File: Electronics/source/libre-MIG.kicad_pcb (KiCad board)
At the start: 2 copper layers, 159.5 x 100.9 mm, 136 parts, among them J1 Conn_01x05, J10 Conn_01x03, J11 Conn_01x08, J12 Conn_01x08, J13 Conn_01x05, J14 Conn_01x03, J15 Conn_01x06, J16 Conn_01x02, J17 Conn_01x06, J18 Conn_01x03, J19 Conn_01x08, J2 Conn_01x03, J20 Conn_01x03, J21 Conn_01x08, J3 Conn_01x03, J4 Conn_01x05, J5 Conn_01x05, J6 Conn_01x20, J7 Conn_01x20, J8 Conn_01x03, J9 Conn_01x03, P1 USB_C_Plug_USB2.0, SW1 SW_Push, SW10 SW_Push, SW11 SW_Push, SW12 SW_Push, SW13 SW_Push, SW14 SW_Coded, SW15 RKJXV1220, SW16 SW_Push, SW17 SKRHABE010, SW18 SKRHABE010, SW2 SW_Push, SW3 SW_Push, SW4 SW_Push, SW5 SW_SPDT, SW6 SW_SPDT, SW7 SW_SPDT, SW8 SW_Push, SW9 SW_Push, U1 STM32F030C8Tx, U2 TCA9535PWR, U3 TCA9535PWR, U4 FT231XS, U5 ADP122AUJZ-3.3-R7, U6 MAX11615EEE, Y1 ABL-32.000MHZ-B2

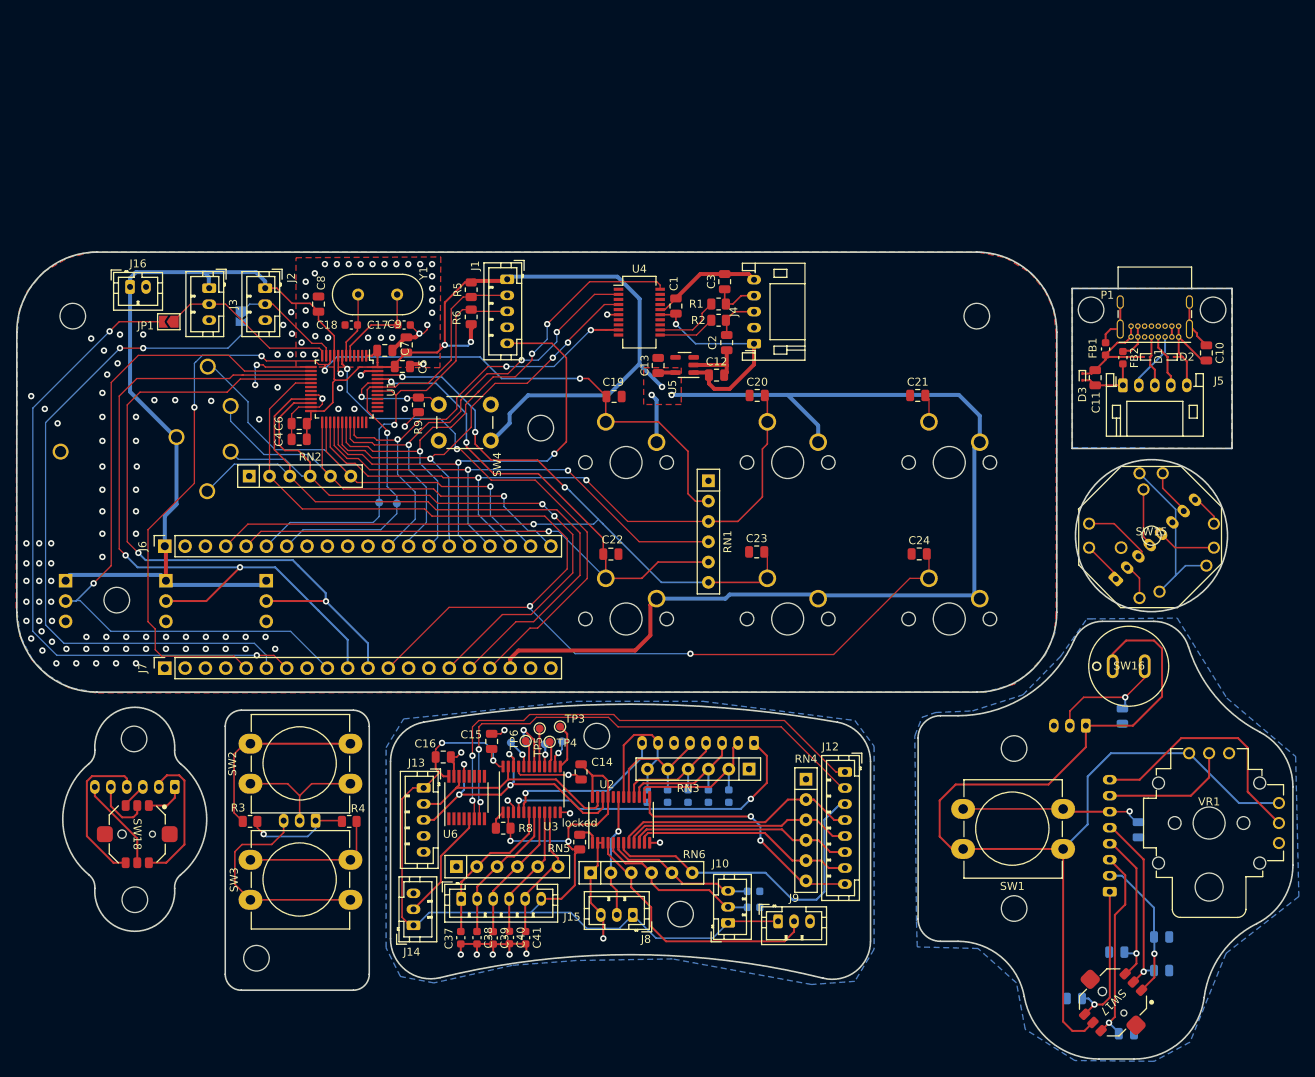
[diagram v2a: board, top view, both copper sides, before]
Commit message: added mechanical ignore
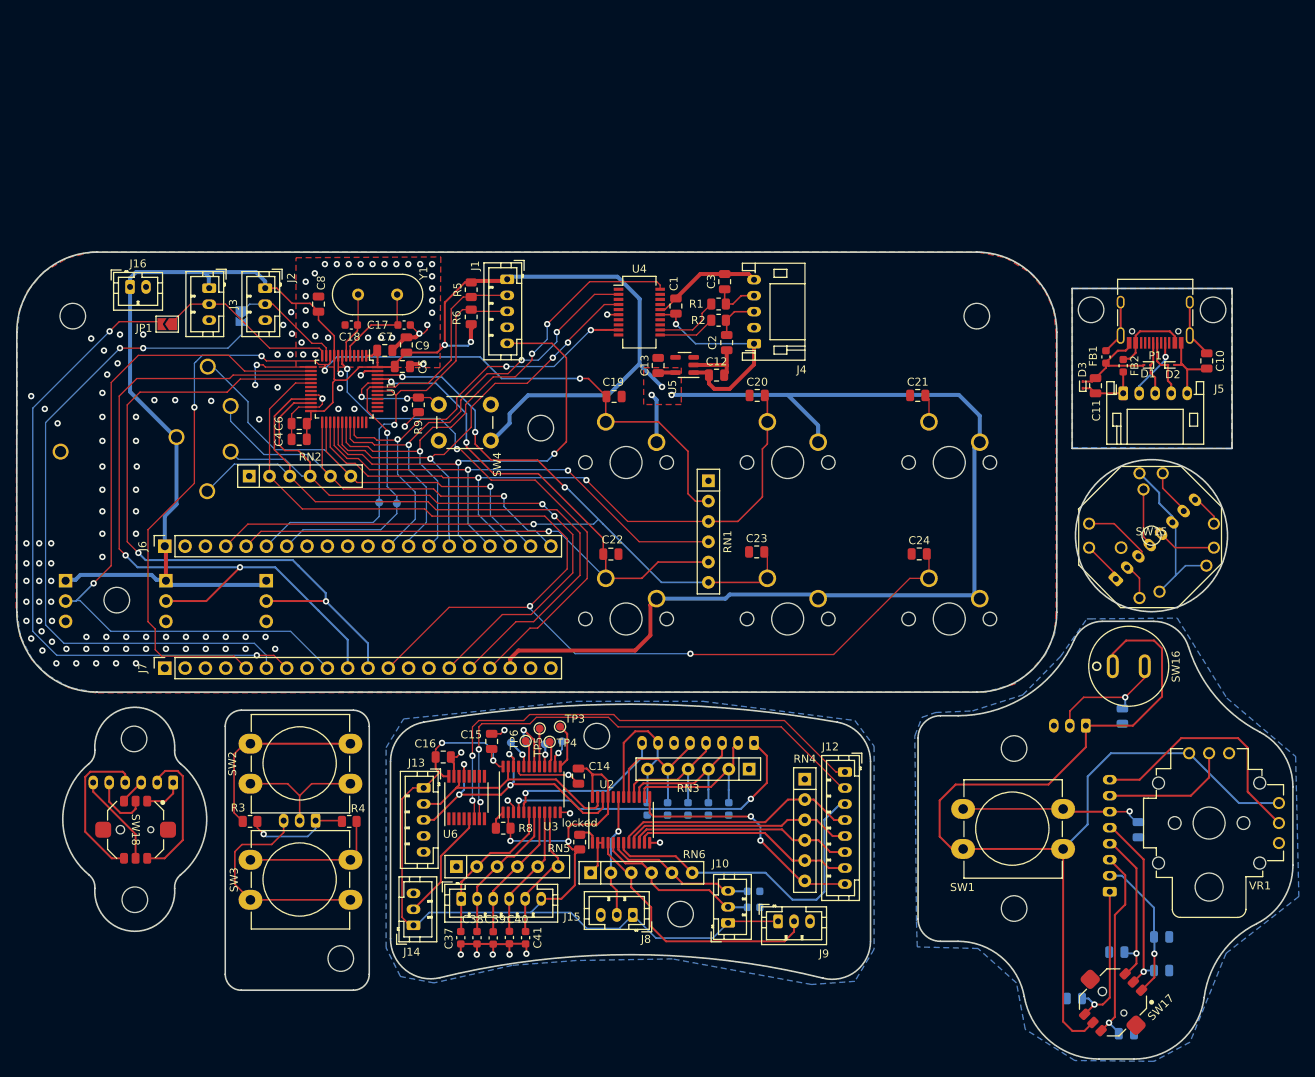
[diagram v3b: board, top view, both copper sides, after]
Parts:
- P1: footprint Connector_USB:USB_C_Receptacle_GCT_USB4085 -> Connector_USB:USB_C_Receptacle_HRO_TYPE-C-31-M-12
- moved REF** 10.5 mm to (157.5, 191.3)
- moved P1 4.41 mm to (259.3, 110.3)
- moved C25 1.60 mm to (200.9, 172.6)
- moved C33 1.60 mm to (203.4, 172.6)
- moved C34 1.60 mm to (198.3, 172.6)
- moved C35 1.60 mm to (195.8, 172.6)
- moved C36 1.60 mm to (206.0, 172.6)
- moved C10 1.00 mm to (265.7, 116.6)
- moved D3 1.00 mm to (250.2, 119.6), turned to 90 degrees
- moved FB1 1.00 mm to (253.1, 116.1)
- moved J5 1.00 mm to (255.3, 120.7)
- moved D1 1.00 mm to (258.3, 117.1), turned to 180 degrees
- moved D2 1.00 mm to (261.3, 117.1), turned to 0 degrees
- moved FB2 1.00 mm to (255.3, 117.2)
- moved C11 1.00 mm to (251.8, 119.7)
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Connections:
- D1 pad 1: GND -> Net-(D1-Pad1)
- D1 pad 2: Net-(D1-Pad2) -> GND
- D2 pad 1: GND -> Net-(D2-Pad1)
- D2 pad 2: Net-(D2-Pad2) -> GND
- D3 pad 1: GND -> +5V
- D3 pad 2: +5V -> GND
- J5 pad 3: Net-(D1-Pad2) -> Net-(D1-Pad1)
- J5 pad 4: Net-(D2-Pad2) -> Net-(D2-Pad1)
- P1 pad A6: Net-(D2-Pad2) -> Net-(D2-Pad1)
- P1 pad A7: Net-(D1-Pad2) -> Net-(D1-Pad1)
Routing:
- net GND: track 145.6 -> 132.2 mm, vias 129 -> 128
- net Net-(D2-Pad1): track 0.00 -> 7.55 mm
- net Net-(D2-Pad2): track 6.70 -> 0.00 mm
- net Net-(D1-Pad1): track 0.00 -> 6.68 mm
- net Net-(D1-Pad2): track 6.35 -> 0.00 mm
- net Net-(FB2-Pad1): track 5.80 -> 10.2 mm
- net /IO Controller/DirL1: track 16.5 -> 18.1 mm
- net /IO Controller/DirU1: track 19.0 -> 20.6 mm
- net /IO Controller/DirR1: track 17.4 -> 19.0 mm
- net /IO Controller/DirC1: track 16.0 -> 17.5 mm
- net /IO Controller/DirD1: track 18.2 -> 19.7 mm
- net Net-(C10-Pad1): track 12.9 -> 14.1 mm
- net unconnected-(J6-Pad11): track 0.73 -> 0.00 mm
- net /MCU/SW5: track 114.1 -> 113.6 mm
- net Net-(J5-Pad2): track 7.41 -> 7.69 mm, vias 0 -> 1
